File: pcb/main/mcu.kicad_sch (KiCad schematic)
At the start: 32 parts, among them J1 UART, J131 I2C, J2 JTAG, J3 JTAG SRC, J4 26 pin IDC, J5 Conn_01x06, SW1 Boot, SW2 Reset, U1 74LVC1G17, U2 74LVC1G17, U3 ESP32-S3-WROOM-1

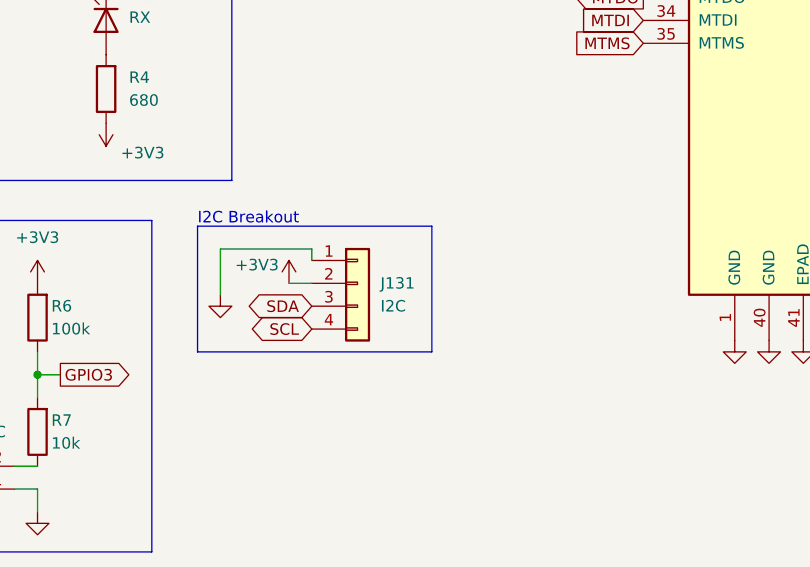
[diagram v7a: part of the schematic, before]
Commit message: Updated schematic and improved make release to reduce manual jlc work
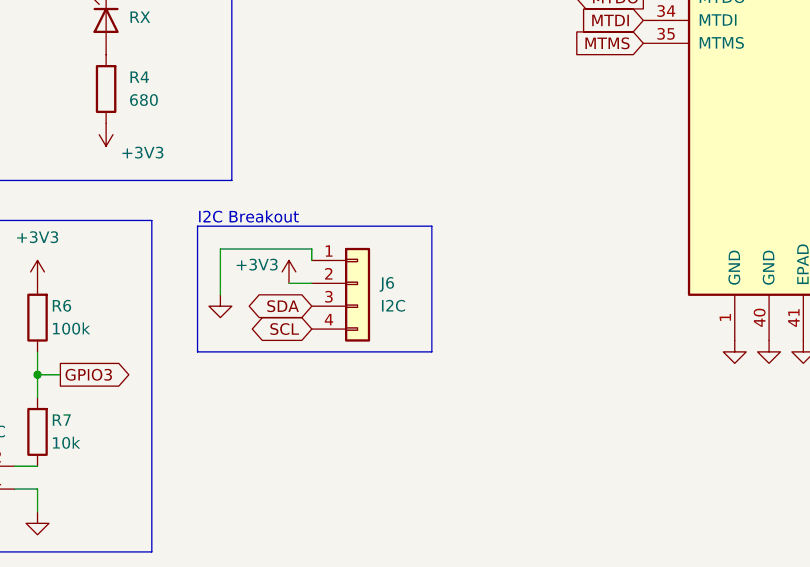
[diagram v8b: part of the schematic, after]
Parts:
- J5: MFG Part No (none) -> S6B-XH-A
- J6: renamed from J131; now left out of the parts list
- U1, U2: MFG Part No (none) -> 74LVC1G17; rotate (none) -> 270
- U3: shift_y (none) -> -3.7mm
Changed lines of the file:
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@@
 			)
 		)
-		(property "MFG Part No" ""
+		(property "MFG Part No" "S6B-XH-A"
 			(at 266.7 41.91 0)
 			(hide yes)
@@
 			)
 		)
-		(property "MFG Part No" ""
+		(property "MFG Part No" "74LVC1G17"
 			(at 50.8 46.99 0)
 			(hide yes)
@@
 			)
 		)
+		(property "rotate" "270"
+			(at 50.8 46.99 0)
+			(hide yes)
+			(show_name no)
+			(do_not_autoplace no)
+			(effects
+				(font
+					(size 1.27 1.27)
+				)
+			)
+		)
 		(pin "3"
 		)
@@
 			)
 		)
+		(property "MFG Part No" "74LVC1G17"
+			(at 60.96 77.47 0)
+			(hide yes)
+			(show_name no)
+			(do_not_autoplace no)
+			(effects
+				(font
+					(size 1.27 1.27)
+				)
+			)
+		)
+		(property "LCSC" ""
+			(at 60.96 77.47 0)
+			(hide yes)
+			(show_name no)
+			(do_not_autoplace no)
+			(effects
+				(font
+					(size 1.27 1.27)
+				)
+			)
+		)
+		(property "rotate" "270"
+			(at 60.96 77.47 0)
+			(hide yes)
+			(show_name no)
+			(do_not_autoplace no)
+			(effects
+				(font
+					(size 1.27 1.27)
+				)
+			)
+		)
 		(pin "3"
 		)
@@
 		(body_style 1)
 		(exclude_from_sim no)
-		(in_bom yes)
+		(in_bom no)
 		(on_board yes)
 		(in_pos_files yes)
 		(dnp no)
 		(fields_autoplaced yes)
-		(property "Reference" "J131"
+		(property "Reference" "J6"
 			(at 101.6 113.0299 0)
 			(show_name no)
@@
 			(project "main"
 				(path "/f225fc02-d36f-4469-bac4-82a576baae3a/0a78e122-cae8-43c8-ae5e-350b0dd676ce"
-					(reference "J131")
+					(reference "J6")
 					(unit 1)
 				)
@@
 			(at 148.59 81.28 0)
 			(hide yes)
+			(show_name no)
+			(do_not_autoplace no)
+			(effects
+				(font
+					(size 1.27 1.27)
+				)
+			)
+		)
+		(property "shift_y" "-3.7mm"
+			(at 148.59 81.28 0)
+			(hide yes)
